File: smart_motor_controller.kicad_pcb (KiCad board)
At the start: 4 copper layers, 85 x 56 mm, 79 parts, among them J10 USB_B_Micro, J101 Breakout, J102 I2C_CONN, J103 CAN_CONN, J104 Debug, J301 M0_CONN, J302 M1_CONN, J303 M2_CONN, J304 M3_CONN, J309 External encoders power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

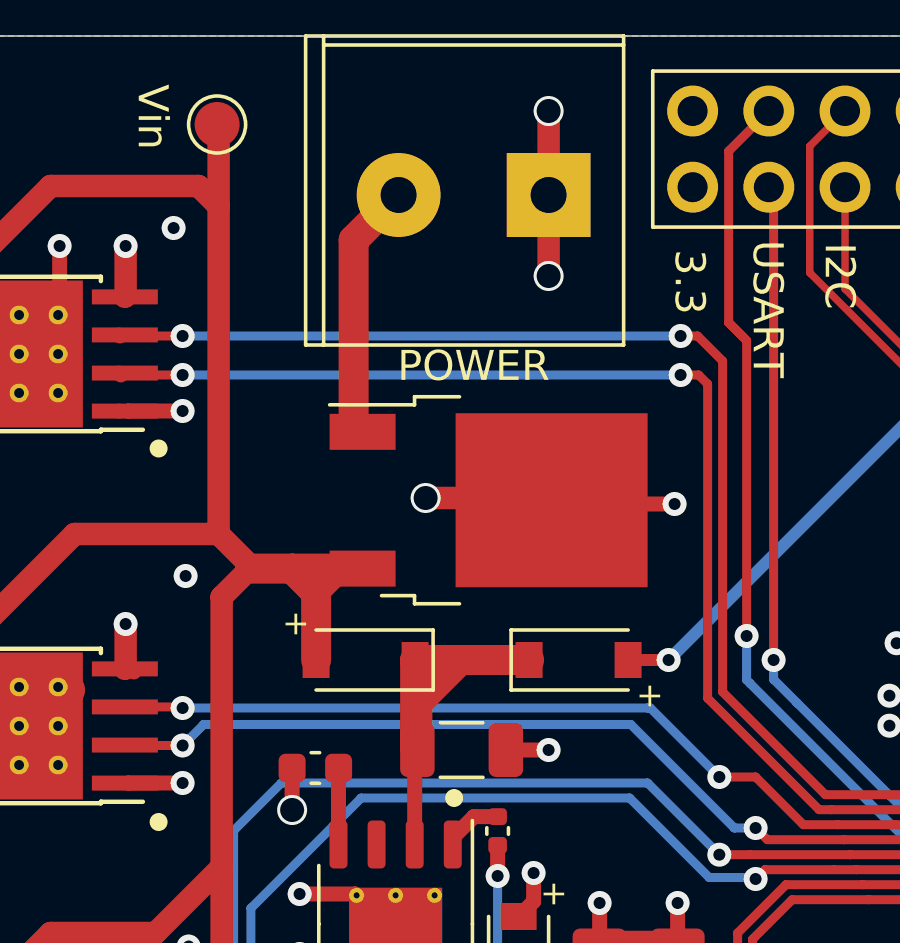
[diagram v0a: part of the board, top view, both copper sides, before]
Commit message: Change in FDD6685
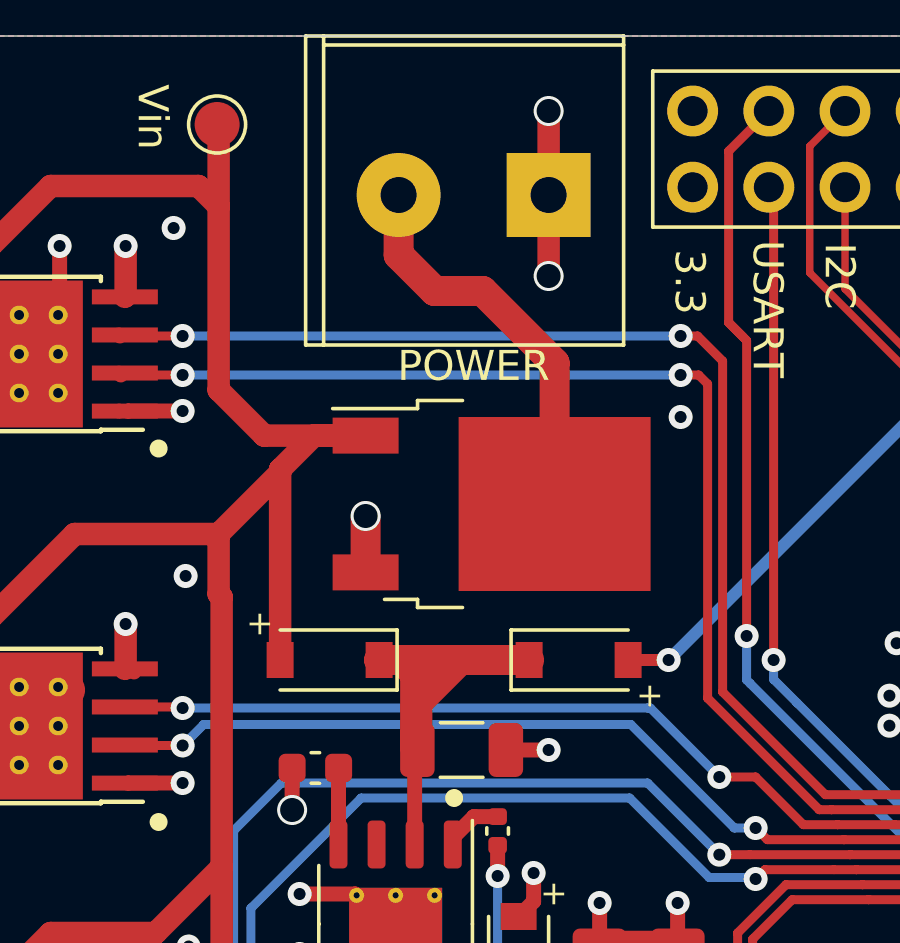
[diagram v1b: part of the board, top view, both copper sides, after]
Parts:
- Q101: footprint Package_TO_SOT_SMD:TO-252-2 -> VsReality_Footprints:FDD6685
- moved D2 1.20 mm to (143.6, 80.9)
- moved Q101 0.16 mm to (149.0, 75.7)
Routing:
- net GND: track 106.8 -> 100.3 mm
- net +12V: track 8.64 -> 13.7 mm
- net BACK_IN: track 13.4 -> 16.0 mm
- net VMOTORS: track 137.7 -> 138.5 mm

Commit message: Update labels on the board
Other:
- board text added: "+12V GND"
- board text added: "0 1"
- board text added: "2 3"
- board text added: "GND 3.3"
- board text added: "Kinisi Motor Controller V0.2.1"
- board text added: "RX"
- board text added: "SDA SCL"
- board text added: "TX"
- board text added: "TX RX"
- board text added: "VIN"
- board text added: "VUSB"
- board text removed: "3.3"
- board text removed: "5V"
- board text removed: "POWER"
- board text removed: "Smart Motor Controller V0.2"
- board text removed: "Vin"
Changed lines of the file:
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@@
   (general
     (thickness 1.6)
-    (drawings 57)
+    (drawings 66)
     (tracks 843)
     (zones 0)
@@
   )
   (setup
-    (last_trace_width 1)
+    (last_trace_width 0.25)
     (user_trace_width 0.3)
     (user_trace_width 0.4)
@@
       (effects (font (size 1 1) (thickness 0.15)))
     )
-    (fp_text user %R (at 0 0) (layer F.Fab)
-      (effects (font (size 1 1) (thickness 0.15)))
-    )
     (fp_line (start 3.95 -2.7) (end 4.95 -2.7) (layer F.Fab) (width 0.1))
     (fp_line (start 4.95 -2.7) (end 4.95 2.7) (layer F.Fab) (width 0.1))
@@
     (fp_line (start 5.55 3.5) (end 5.55 -3.5) (layer F.CrtYd) (width 0.05))
     (fp_line (start 5.55 -3.5) (end -5.55 -3.5) (layer F.CrtYd) (width 0.05))
+    (fp_text user %R (at 0 0) (layer F.Fab)
+      (effects (font (size 1 1) (thickness 0.15)))
+    )
     (pad "" smd rect (at 0.425 1.525) (size 3.05 2.75) (layers F.Paste))
     (pad "" smd rect (at 3.775 -1.525) (size 3.05 2.75) (layers F.Paste))
@@
     )
   )
+  (gr_text I2C (at 160.6 67.4 270) (layer B.SilkS)
+    (effects (font (size 1 1) (thickness 0.15)) (justify mirror))
+  )
+  (gr_text USART (at 158.2 68.6 270) (layer B.SilkS)
+    (effects (font (size 1 1) (thickness 0.15)) (justify mirror))
+  )
+  (gr_text TX (at 195.1 104.1) (layer B.SilkS)
+    (effects (font (size 1 1) (thickness 0.15)) (justify mirror))
+  )
+  (gr_text RX (at 195.1 102.3) (layer B.SilkS)
+    (effects (font (size 1 1) (thickness 0.15)) (justify mirror))
+  )
+  (gr_text GND (at 163.4 109.9 270) (layer F.SilkS)
+    (effects (font (size 1 1) (thickness 0.15)))
+  )
+  (gr_text "GND 3.3" (at 168.4 68.9 270) (layer F.SilkS)
+    (effects (font (size 0.8 0.7) (thickness 0.12)))
+  )
+  (gr_text "0 1" (at 165.8 69.1 270) (layer F.SilkS)
+    (effects (font (size 0.8 0.7) (thickness 0.12)))
+  )
+  (gr_text "2 3" (at 163.2 69.1 270) (layer F.SilkS)
+    (effects (font (size 0.8 0.7) (thickness 0.12)))
+  )
+  (gr_line (start 154.6 69.1) (end 169.8 69.1) (layer F.SilkS) (width 0.15))
   (gr_circle (center 182.8 92.5) (end 182.65 92.5) (layer F.SilkS) (width 0.3))
   (gr_circle (center 147.75 85.5) (end 147.75 85.65) (layer F.SilkS) (width 0.3))
@@
     (effects (font (size 0.8 0.8) (thickness 0.15)))
   )
-  (gr_text USART (at 158.2 69.2 270) (layer F.SilkS)
-    (effects (font (size 1 1) (thickness 0.15)))
+  (gr_text "TX RX" (at 158.2 69.1 270) (layer F.SilkS)
+    (effects (font (size 0.8 0.7) (thickness 0.12)))
   )
   (gr_text CLK (at 185.26 65.8 270) (layer F.SilkS)
@@
     (effects (font (size 1 1) (thickness 0.15)))
   )
-  (gr_text I2C (at 160.6 68.1 270) (layer F.SilkS)
-    (effects (font (size 1 1) (thickness 0.15)))
+  (gr_text "SDA SCL" (at 160.6 69.1 270) (layer F.SilkS)
+    (effects (font (size 0.8 0.7) (thickness 0.12)))
   )
   (gr_text B (at 143.4 108.8) (layer F.SilkS)
@@
     (effects (font (size 0.9 0.9) (thickness 0.15)))
   )
-  (gr_text "Smart Motor\nController\nV0.2" (at 163.9 102.1) (layer F.SilkS)
+  (gr_text "Kinisi Motor\nController\nV0.2.1" (at 163.9 102.1) (layer F.SilkS)
     (effects (font (size 1.2 1.2) (thickness 0.15)) (justify left))
   )
@@
     (effects (font (size 1 1) (thickness 0.15)))
   )
-  (gr_text POWER (at 148.4 71.1) (layer F.SilkS)
+  (gr_text "+12V GND" (at 148.4 71.1) (layer F.SilkS)
     (effects (font (size 1 1) (thickness 0.15)))
   )
@@
     (effects (font (size 1 1) (thickness 0.15)))
   )
-  (gr_text Vin (at 137.7 62.8 270) (layer F.SilkS)
+  (gr_text VIN (at 137.7 62.8 270) (layer F.SilkS)
     (effects (font (size 1 1) (thickness 0.15)))
   )
-  (gr_text 5V (at 184.8 81.8) (layer F.SilkS)
+  (gr_text VUSB (at 184.8 82.7 270) (layer F.SilkS)
     (effects (font (size 1 1) (thickness 0.15)))
   )
-  (gr_text VE (at 164.65 110.6) (layer F.SilkS)
+  (gr_text VE (at 166 110.5 270) (layer F.SilkS)
     (effects (font (size 1 1) (thickness 0.15)))
   )
-  (gr_text 3.3 (at 155.6 68.3 270) (layer F.SilkS)
-    (effects (font (size 1 1) (thickness 0.15)))
+  (gr_text "GND 3.3" (at 155.6 68.9 270) (layer F.SilkS)
+    (effects (font (size 0.8 0.7) (thickness 0.12)))
   )
   (gr_text GND (at 187.8 65.9 270) (layer F.SilkS)

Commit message: Initial update
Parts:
- removed H1, H2, H3, H4, H5, H6: MountingHole_Pad, MountingHole:MountingHole_2.7mm_M2.5_Pad
- removed Q101: FDD6685, VsReality_Footprints:FDD6685
- added H201: MountingHole_Pad, MountingHole:MountingHole_2.7mm_M2.5_Pad, F.Cu at (115.8, 63.3)
- added H202: MountingHole_Pad, MountingHole:MountingHole_2.7mm_M2.5_Pad, F.Cu at (194.2, 63.3)
- added H203: MountingHole_Pad, MountingHole:MountingHole_2.7mm_M2.5_Pad, F.Cu at (194.2, 112.7)
- added H204: MountingHole_Pad, MountingHole:MountingHole_2.7mm_M2.5_Pad, F.Cu at (115.8, 112.7)
- J102: footprint Connector_JST:JST_PH_S4B-PH-SM4-TB_1x04-1MP_P2.00mm_Horizontal -> Connector_JST:JST_PH_B4B-PH-K_1x04_P2.00mm_Vertical
- J103: footprint Connector_JST:JST_PH_S2B-PH-SM4-TB_1x02-1MP_P2.00mm_Horizontal -> Connector_JST:JST_PH_B2B-PH-K_1x02_P2.00mm_Vertical
- J9: footprint VsReality_Footprints:Ningbo_Kangnex_Elec_WJ128V_5_0_2P -> Connector_AMASS:AMASS_XT30UPB-M_1x02_P5.0mm_Vertical
- moved J10 80.0 mm to (115.1, 74.9), turned to -90 degrees
- moved 3.3V201 74.0 mm to (115.3, 96.6)
- moved J304 67.4 mm to (184.7, 110.7), turned to 0 degrees
- moved U3 64.0 mm to (123.1, 73.8), turned to 0 degrees
- moved R304 62.6 mm to (190.1, 100.4), turned to -90 degrees
- moved TP2 61.5 mm to (123.5, 78.8), turned to 90 degrees
- moved J302 59.7 mm to (174.7, 110.7), turned to 0 degrees
- moved C308 58.6 mm to (185.9, 101.0), turned to -90 degrees
- moved U304 57.2 mm to (189.5, 94.5), turned to -90 degrees
- moved J104 55.4 mm to (132.5, 62.2)
- moved C307 54.6 mm to (185.2, 97.5), turned to 0 degrees
- moved J303 54.5 mm to (164.7, 110.7), turned to 0 degrees
- moved SW102 54.0 mm to (148.4, 62.7), turned to 0 degrees
- moved J301 52.8 mm to (154.7, 110.7), turned to 0 degrees
- moved C17 51.2 mm to (134.3, 71.2), turned to 0 degrees
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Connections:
- J10 pad 4: Net-(J10-Pad4) -> unconnected-(J10-ID-Pad4)
- J10 pad 6: Net-(J10-Pad6) -> unconnected-(J10-Shield-Pad6)
- J9 pad 2: +12V -> VMOTORS
- U2 pad 10: Net-(U2-Pad10) -> unconnected-(U2-PC2-Pad10)
- U2 pad 11: Net-(U2-Pad11) -> unconnected-(U2-PC3-Pad11)
- U2 pad 2: Net-(U2-Pad2) -> unconnected-(U2-PC13-Pad2)
- U2 pad 24: Net-(U2-Pad24) -> unconnected-(U2-PC4-Pad24)
- U2 pad 25: Net-(U2-Pad25) -> unconnected-(U2-PC5-Pad25)
- U2 pad 26: Net-(U2-Pad26) -> unconnected-(U2-PB0-Pad26)
- U2 pad 27: Net-(U2-Pad27) -> unconnected-(U2-PB1-Pad27)
- U2 pad 28: Net-(U2-Pad28) -> unconnected-(U2-PB2-Pad28)
- U2 pad 3: Net-(U2-Pad3) -> unconnected-(U2-PC14-Pad3)
- U2 pad 4: Net-(U2-Pad4) -> unconnected-(U2-PC15-Pad4)
- U2 pad 43: Net-(U2-Pad43) -> unconnected-(U2-PA10-Pad43)
- U2 pad 54: Net-(U2-Pad54) -> unconnected-(U2-PD2-Pad54)
- U2 pad 56: Net-(U2-Pad56) -> unconnected-(U2-PB4-Pad56)
- U2 pad 57: Net-(U2-Pad57) -> unconnected-(U2-PB5-Pad57)
- U2 pad 8: Net-(U2-Pad8) -> unconnected-(U2-PC0-Pad8)
- U2 pad 9: Net-(U2-Pad9) -> unconnected-(U2-PC1-Pad9)
- U201 pad 3: Net-(U201-Pad3) -> unconnected-(U201-EN-Pad3)
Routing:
- net ENCODER_1_B: track 42.2 -> 0.00 mm, vias 1 -> 0
- net SWCLK: track 41.4 -> 0.34 mm, vias 2 -> 0
- net ENCODER_1_A: track 39.8 -> 0.00 mm, vias 1 -> 0
- net +5V: track 50.4 -> 12.4 mm, vias 2 -> 0
- net USART3_TX: track 36.5 -> 0.00 mm, vias 2 -> 0
- net SWDIO: track 38.3 -> 2.81 mm, vias 2 -> 0
- net M3_OUT2: track 40.9 -> 6.31 mm
- net CAN2_TX: track 38.8 -> 4.45 mm, vias 2 -> 0
- net M0_OUT1: track 39.7 -> 5.49 mm, vias 2 -> 1
- net M3_OUT1: track 40.6 -> 7.08 mm
- net M0_OUT2: track 39.1 -> 5.75 mm, vias 2 -> 1
- net ENCODER_3_B: track 40.7 -> 7.59 mm, vias 2 -> 0
- net ENCODER_2_B: track 33.1 -> 0.00 mm
- net USART3_RX: track 32.5 -> 0.36 mm, vias 2 -> 0
- net CAN2_RX: track 38.3 -> 6.91 mm, vias 2 -> 0
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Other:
- net class Default removed
- board text added: "Kinisi Motor Controller V0.3"
- board text removed: "Kinisi Motor Controller V0.2.1"

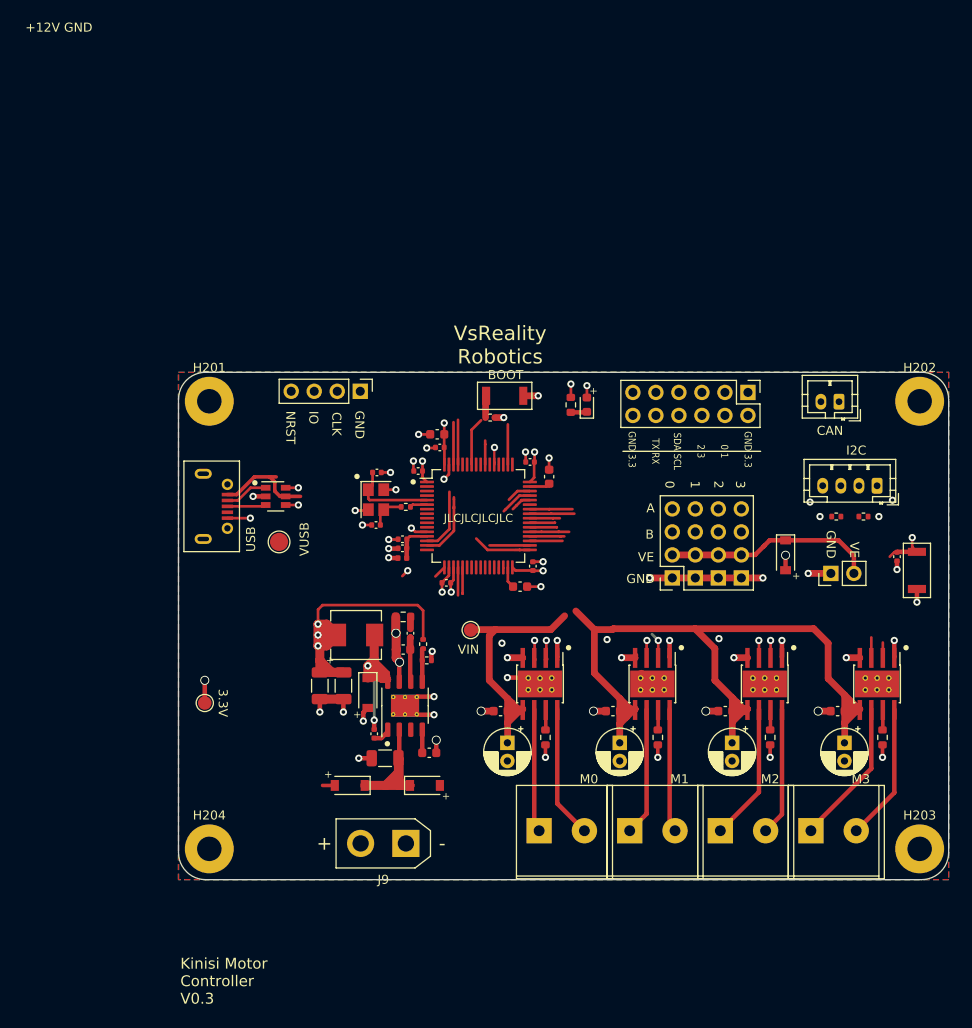
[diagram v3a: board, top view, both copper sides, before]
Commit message: Edge of the bpard
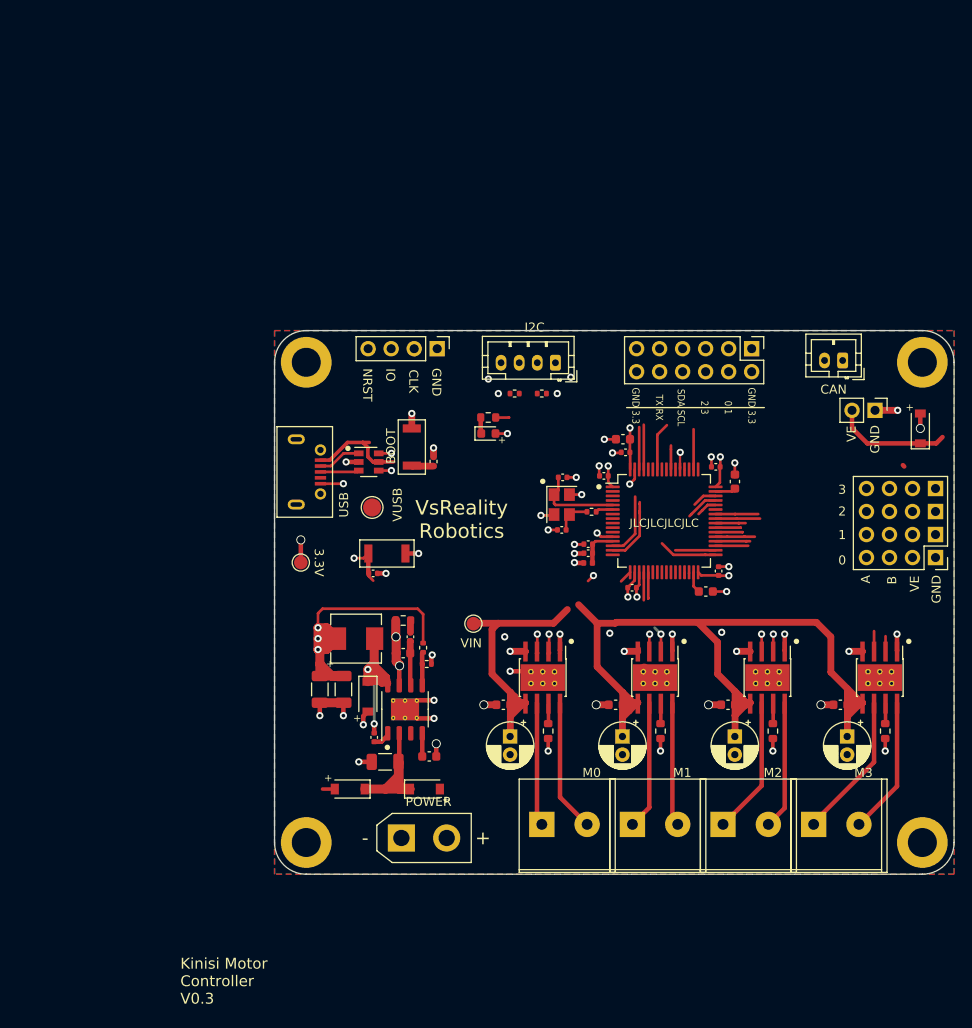
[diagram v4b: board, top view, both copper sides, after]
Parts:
- H201, H202, H203, H204: footprint MountingHole:MountingHole_2.7mm_M2.5_Pad -> MountingHole:MountingHole_3.2mm_M3_DIN965_Pad
- moved SW103 58.5 mm to (135.4, 80.1), turned to 180 degrees
- moved C101 57.8 mm to (133.9, 82.3), turned to 0 degrees
- moved J102 38.0 mm to (154.0, 59.0)
- moved R14 38.0 mm to (152.5, 62.5)
- moved R15 38.0 mm to (149.5, 62.5)
- moved J310 29.1 mm to (195.9, 80.5), turned to 180 degrees
- moved C13 20.5 mm to (157.6, 80.1)
- moved C14 20.5 mm to (157.6, 79.1)
- moved C15 20.5 mm to (170.6, 84.3)
- moved C16 20.5 mm to (173.8, 72.2)
- moved C17 20.5 mm to (154.8, 71.7)
- moved C3 20.5 mm to (161.5, 67.5)
- moved C4 20.5 mm to (159.3, 71.5)
- moved C5 20.5 mm to (162.5, 83.9)
- moved C6 20.5 mm to (172.0, 82.0)
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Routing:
- net GND: track 89.4 -> 76.9 mm, vias 52 -> 49
- net V_ENCODER: track 23.6 -> 13.2 mm
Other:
- board size 85 x 56 mm -> 75 x 60 mm
- board text added: "POWER"
- board text removed: "+12V GND"
